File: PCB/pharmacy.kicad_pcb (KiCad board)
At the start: 2 copper layers, 111 x 98 mm, 10 parts, among them J1 PWR_Conn, U1 ctrlr_TL, U2 LEDs_T, U3 ctrlr_BR, U4 LEDs_B, U5 LEDs_R, U6 LEDs_L, U7 ctrlr_C, U8 ESP32-C6-DEVKITC-1-N8, U9 LEDs_C

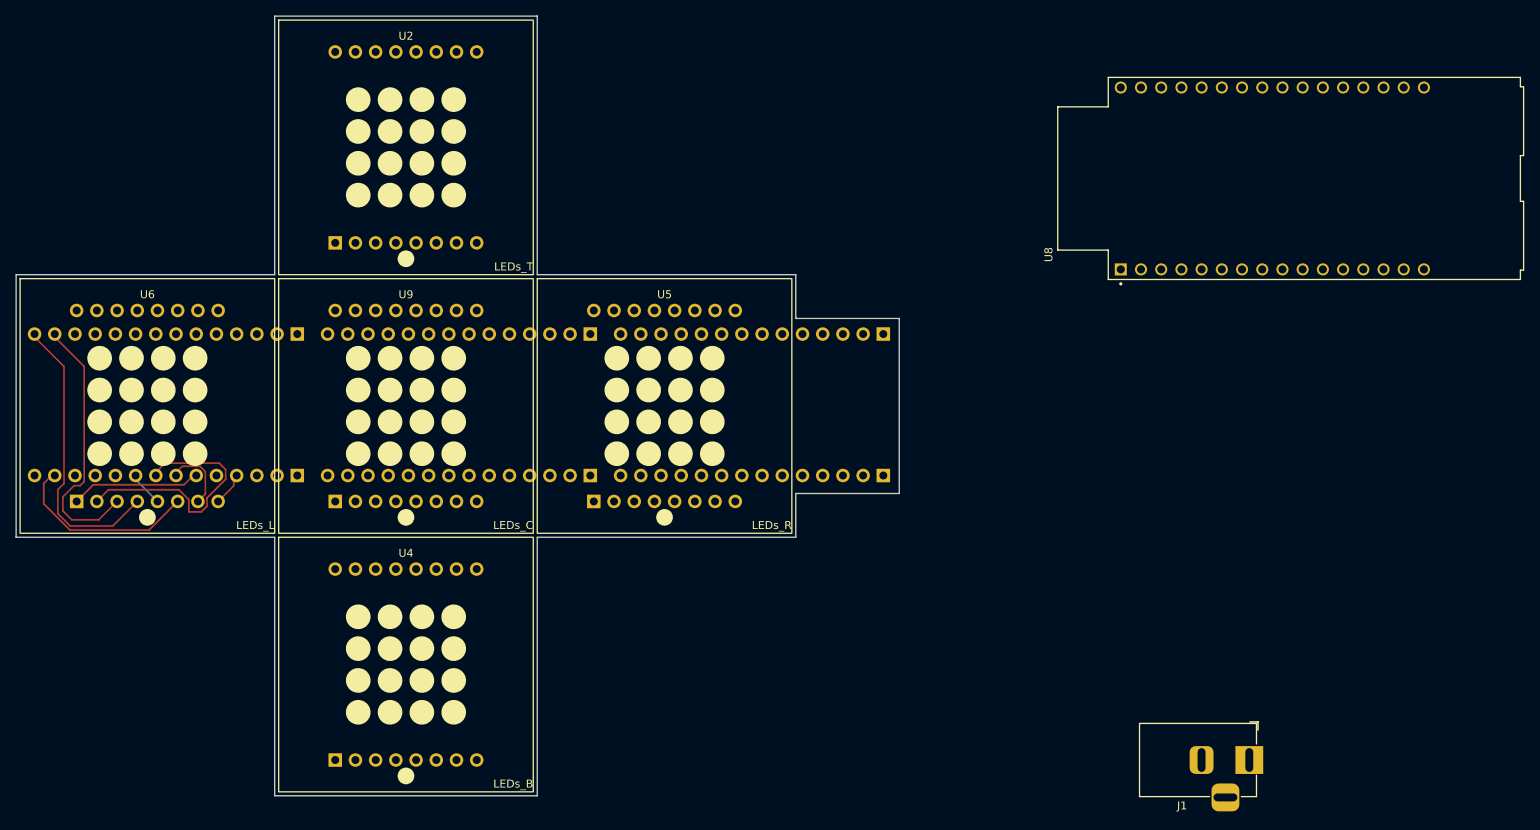
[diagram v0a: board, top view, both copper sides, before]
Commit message: Added mounting holes to PCB
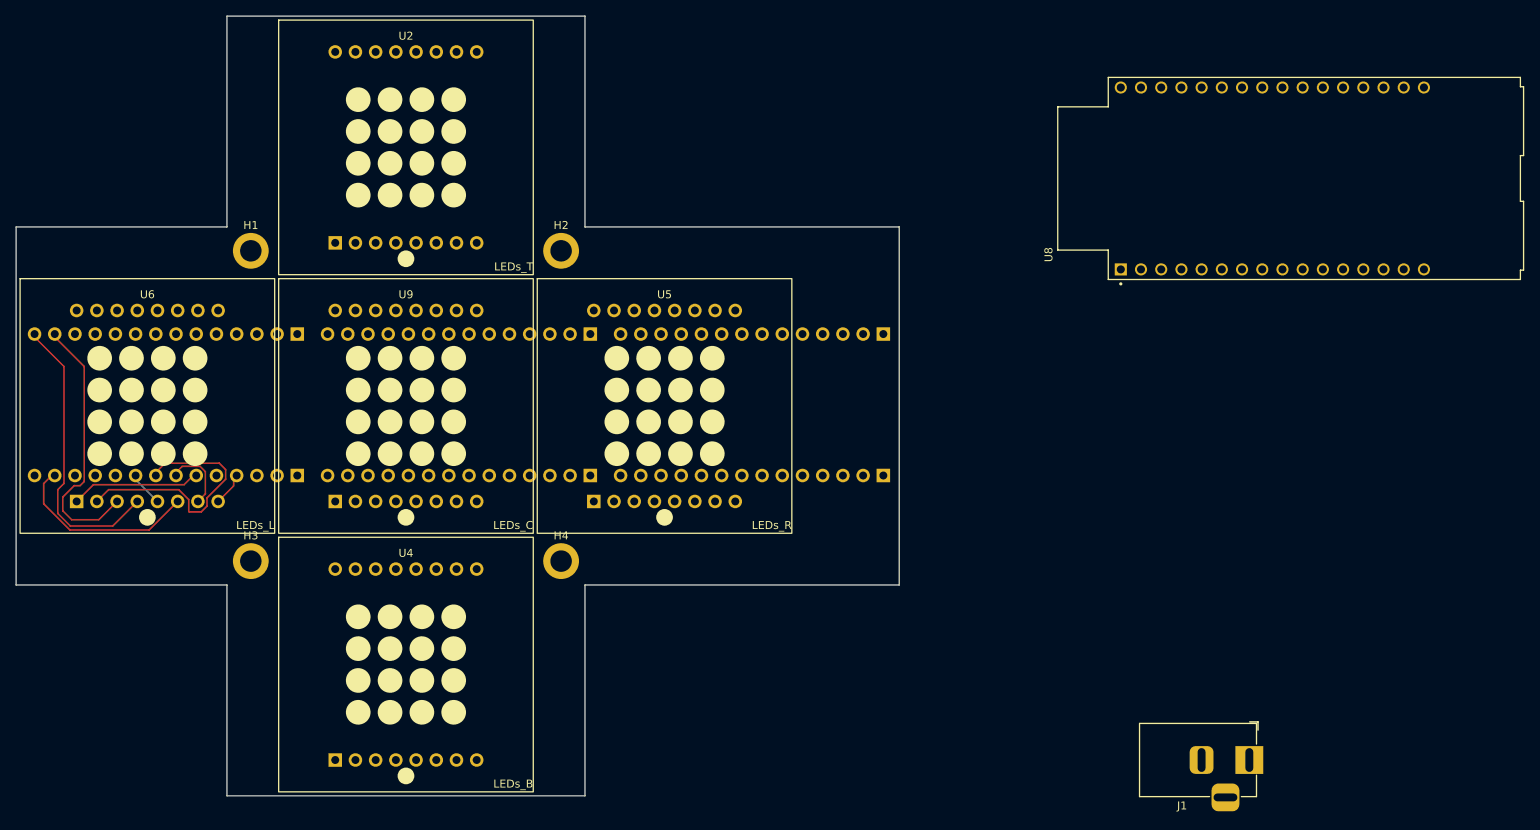
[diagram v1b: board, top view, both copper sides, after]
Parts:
- added H1: MountingHole_Pad, MountingHole:MountingHole_2.7mm_M2.5_ISO7380_Pad, F.Cu at (119.0, 66.5)
- added H2: MountingHole_Pad, MountingHole:MountingHole_2.7mm_M2.5_ISO7380_Pad, F.Cu at (158.0, 66.5)
- added H3: MountingHole_Pad, MountingHole:MountingHole_2.7mm_M2.5_ISO7380_Pad, F.Cu at (119.0, 105.5)
- added H4: MountingHole_Pad, MountingHole:MountingHole_2.7mm_M2.5_ISO7380_Pad, F.Cu at (158.0, 105.5)
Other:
- outline, holes or cut-outs redrawn
